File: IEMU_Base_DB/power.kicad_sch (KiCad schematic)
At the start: 47 parts, among them J101 USB4125-GF-A, J102 Conn_01x02_Pin, Q101 CSD85301Q2, U101 NPM1300-QEAA-R7, U102 BQ29702DSER, U103 TPS61099DRV, U104 INA216A2RSWR

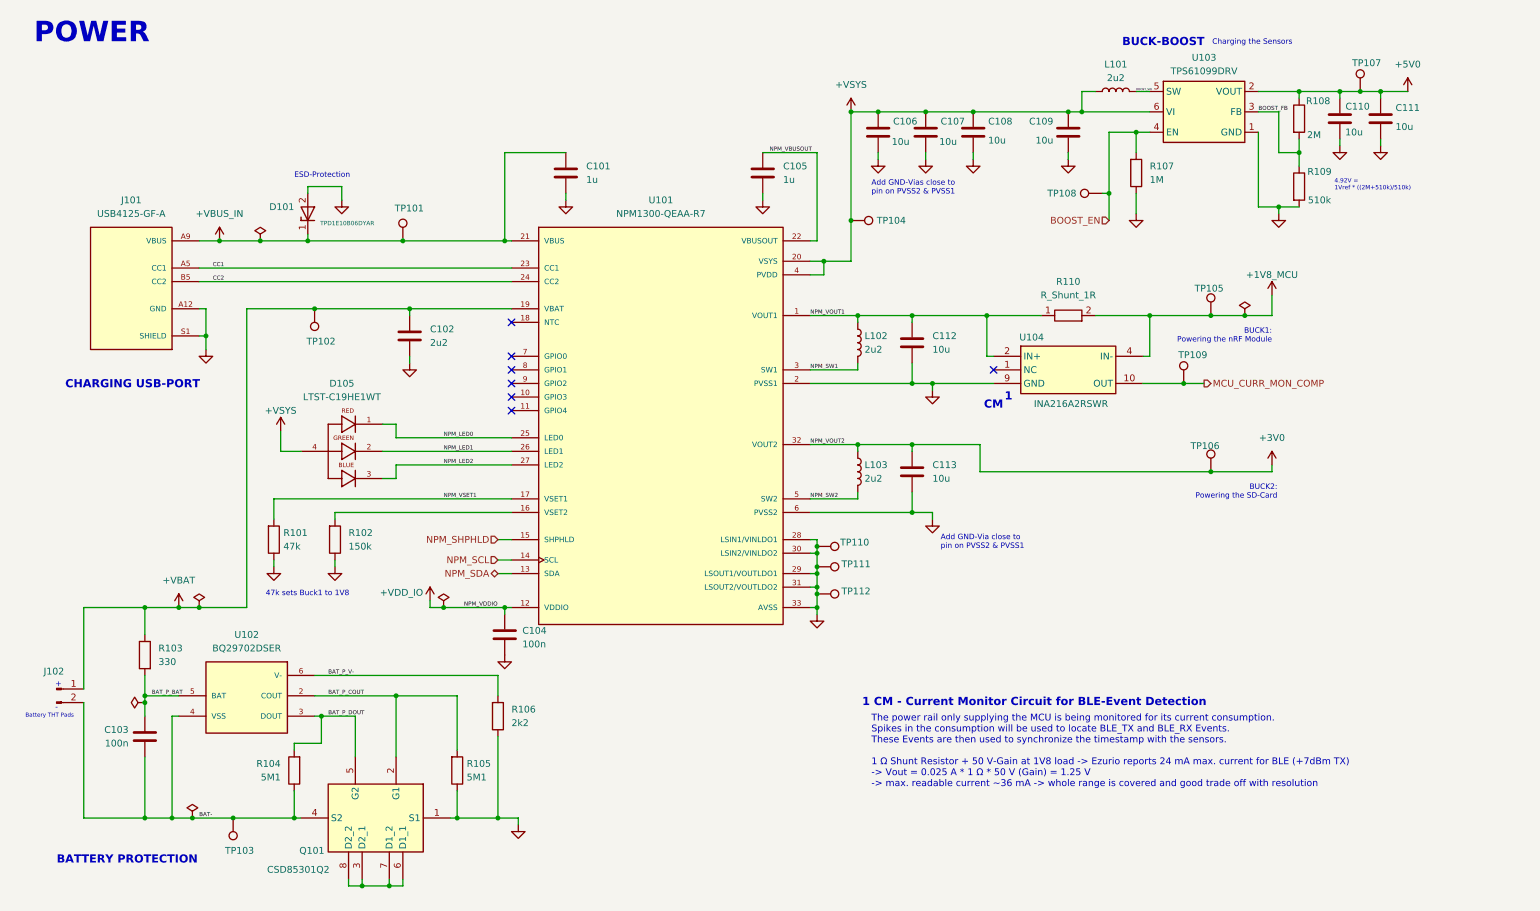
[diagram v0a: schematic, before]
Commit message: implemented changes from the review with TF and fixed lost parts in the library
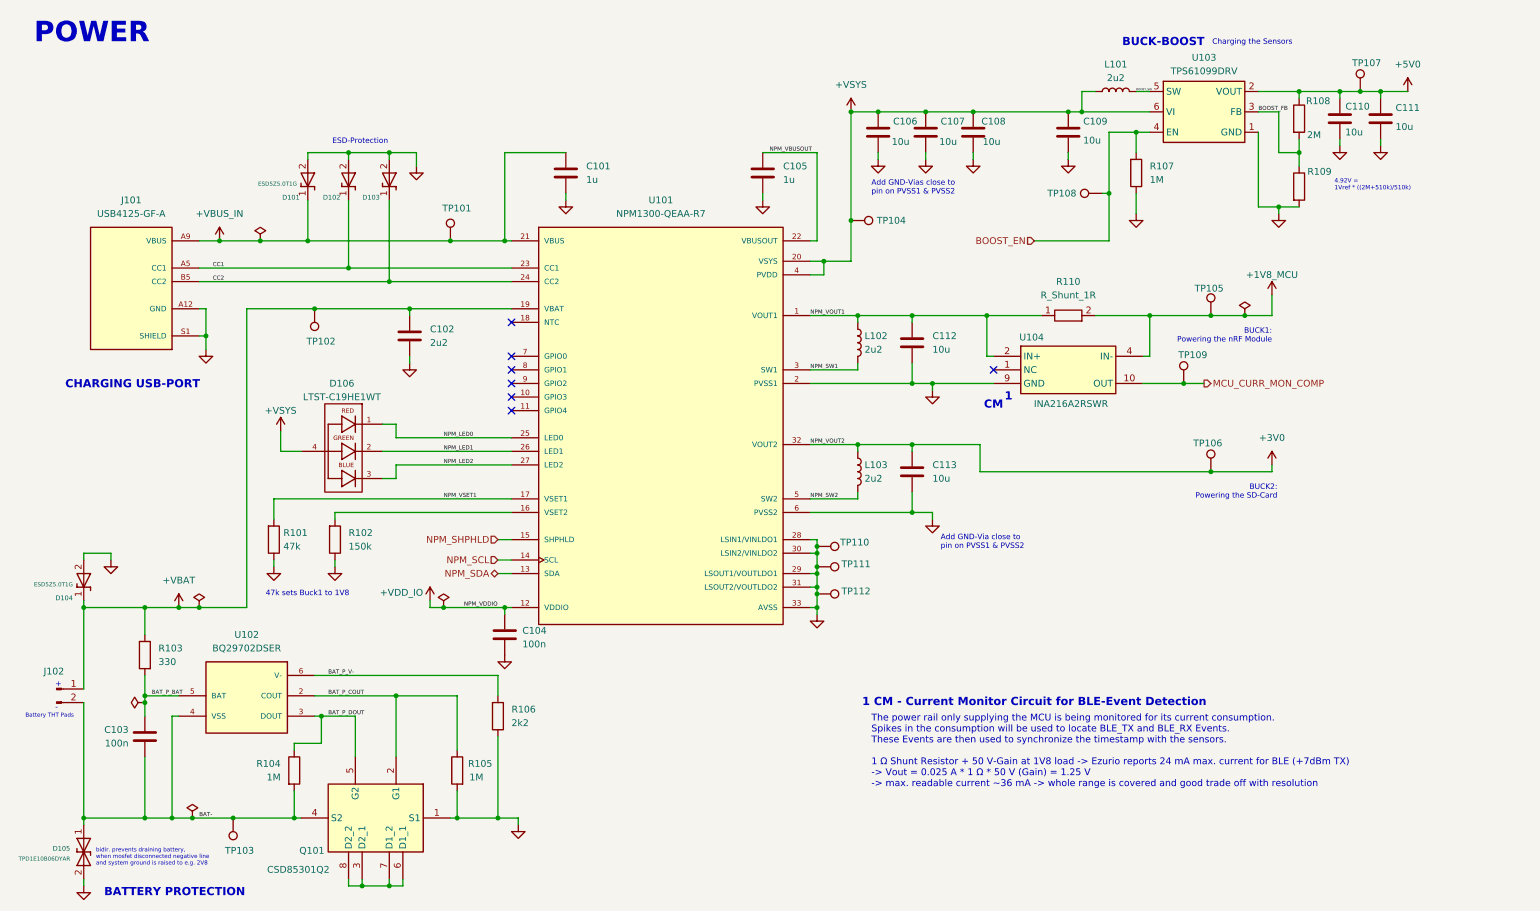
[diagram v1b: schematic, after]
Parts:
- removed D101: TPD1E10B06DYAR, Diode_SMD:D_SOD-523, symbol 0_Power:TPD1E10B06DYAR
- removed J101: USB4125-GF-A, 0_Connectors:GCT_USB4125-GF-A_REVA2, symbol 0_Connectors:USB4125-GF-A
- removed R104, R105: 5M1, Resistor_SMD:R_0402_1005Metric, symbol 0_Passives:R_5M1
- added D101, D102, D103, D104: ESD5Z5.0T1G, Diode_SMD:D_SOD-523_1, symbol 0_Power:ESD5Z5.0T1G
- added D105: TPD1E10B06DYAR, Diode_SMD:D_SOD-523, symbol 0_Power:TPD1E10B06DYAR
- added J101: USB4125-GF-A, 0_Connectors:GCT_USB4125-GF-A_REVA2, symbol 0_Connectors:USB4125-GF-A_REVA2
- added R104, R105: 1M, Resistor_SMD:R_0402_1005Metric, symbol 0_Passives:R_1M
- D106: renamed from D105; Distributer Link 1 https://www.mouser.de/ProductDetail/LITEON/LTST-C19HE1WT?qs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 -> (none); Distributor Link 1 (none) -> https://www.mouser.de/ProductDetail/LITEON/LTST-C19HE1WT?qs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
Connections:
- net +VBAT: now also D104.1 (I/O)
- net +VBUS_IN: now also D101.1 (I/O), J101.A9 (VBUS), J101.B9 (VBUS)
- net BAT-: now also D105.1 (I/O), R104.1
- net BAT_P_COUT: now also R105.2
- net BAT_P_DOUT: now also R104.2
- net CC1: now also D102.1 (I/O), J101.A5 (CC1)
- net CC2: now also D103.1 (I/O), J101.B5 (CC2)
- net GND: now also D101.2 (GND), D102.2 (GND), D103.2 (GND), D104.2 (GND), D105.2 (GND), J101.A12 (GND), J101.B12 (GND), J101.S1 (SHIELD), J101.S2 (SHIELD), J101.S3 (SHIELD), J101.S4 (SHIELD), R105.1
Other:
- note added: "Add GND-Via close to pin on PVSS1 & PVSS2"
- note added: "Add GND-Vias close to pin on PVSS1 & PVSS2"
- note added: "bidir. prevents draining battery, when mosfet disconnected negative line and system ground is raised to e.g. 2V8"
- note removed: "Add GND-Via close to pin on PVSS2 & PVSS1"
- note removed: "Add GND-Vias close to pin on PVSS2 & PVSS1"
- moved on the sheet: TP101

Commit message: layout of base and some fixes on the sensor layout
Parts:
- TP101, TP102, TP103, TP104, TP105, TP106, TP107, TP108, TP109, TP110, TP111, TP112: footprint TestPoint:TestPoint_Pad_D2.0mm -> TestPoint:TestPoint_Pad_D1.0mm
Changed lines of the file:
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@@
 			)
 		)
-		(property "Footprint" "TestPoint:TestPoint_Pad_D2.0mm"
+		(property "Footprint" "TestPoint:TestPoint_Pad_D1.0mm"
 			(at 62.23 170.18 0)
 			(effects
@@
 			)
 		)
-		(property "Footprint" "TestPoint:TestPoint_Pad_D2.0mm"
+		(property "Footprint" "TestPoint:TestPoint_Pad_D1.0mm"
 			(at 166.37 128.27 0)
 			(effects
@@
 			)
 		)
-		(property "Footprint" "TestPoint:TestPoint_Pad_D2.0mm"
+		(property "Footprint" "TestPoint:TestPoint_Pad_D1.0mm"
 			(at 245.11 105.41 0)
 			(effects
@@
 			)
 		)
-		(property "Footprint" "TestPoint:TestPoint_Pad_D2.0mm"
+		(property "Footprint" "TestPoint:TestPoint_Pad_D1.0mm"
 			(at 166.37 124.46 0)
 			(effects
@@
 			)
 		)
-		(property "Footprint" "TestPoint:TestPoint_Pad_D2.0mm"
+		(property "Footprint" "TestPoint:TestPoint_Pad_D1.0mm"
 			(at 273.05 34.29 0)
 			(effects
@@
 			)
 		)
-		(property "Footprint" "TestPoint:TestPoint_Pad_D2.0mm"
+		(property "Footprint" "TestPoint:TestPoint_Pad_D1.0mm"
 			(at 77.47 74.93 0)
 			(effects
@@
 			)
 		)
-		(property "Footprint" "TestPoint:TestPoint_Pad_D2.0mm"
+		(property "Footprint" "TestPoint:TestPoint_Pad_D1.0mm"
 			(at 240.03 88.9 0)
 			(effects
@@
 			)
 		)
-		(property "Footprint" "TestPoint:TestPoint_Pad_D2.0mm"
+		(property "Footprint" "TestPoint:TestPoint_Pad_D1.0mm"
 			(at 219.71 58.42 0)
 			(effects
@@
 			)
 		)
-		(property "Footprint" "TestPoint:TestPoint_Pad_D2.0mm"
+		(property "Footprint" "TestPoint:TestPoint_Pad_D1.0mm"
 			(at 102.87 62.23 0)
 			(effects
@@
 			)
 		)
-		(property "Footprint" "TestPoint:TestPoint_Pad_D2.0mm"
+		(property "Footprint" "TestPoint:TestPoint_Pad_D1.0mm"
 			(at 166.37 133.35 0)
 			(effects
@@
 			)
 		)
-		(property "Footprint" "TestPoint:TestPoint_Pad_D2.0mm"
+		(property "Footprint" "TestPoint:TestPoint_Pad_D1.0mm"
 			(at 172.72 53.34 0)
 			(effects
@@
 			)
 		)
-		(property "Footprint" "TestPoint:TestPoint_Pad_D2.0mm"
+		(property "Footprint" "TestPoint:TestPoint_Pad_D1.0mm"
 			(at 245.11 76.2 0)
 			(effects
